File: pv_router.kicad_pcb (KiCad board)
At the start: 4 copper layers, 75 x 69.2 mm, 51 parts, among them IC1 L6981C33DR, IC2 ATM90E26-YU-B, IC3 ESP32-C3-WROOM-02-N4, J1 Barrel_Jack_Switch_Pin3Ring, J2 AudioJack3, J3 AudioJack3, J4 Barrel_Jack_Switch_Pin3Ring, J5 UART, J6 ToSSR, Q1 BSS138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

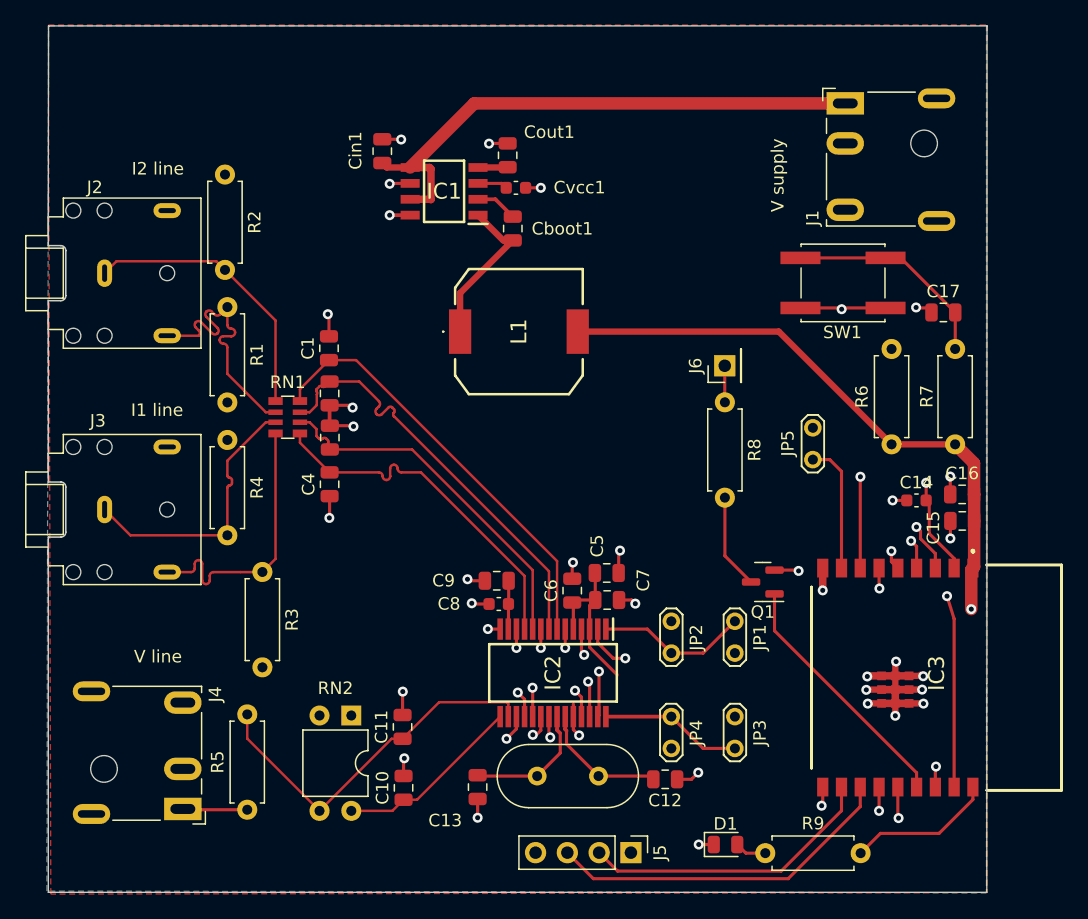
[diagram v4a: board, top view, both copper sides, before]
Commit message: pcb: add GND vias in planes
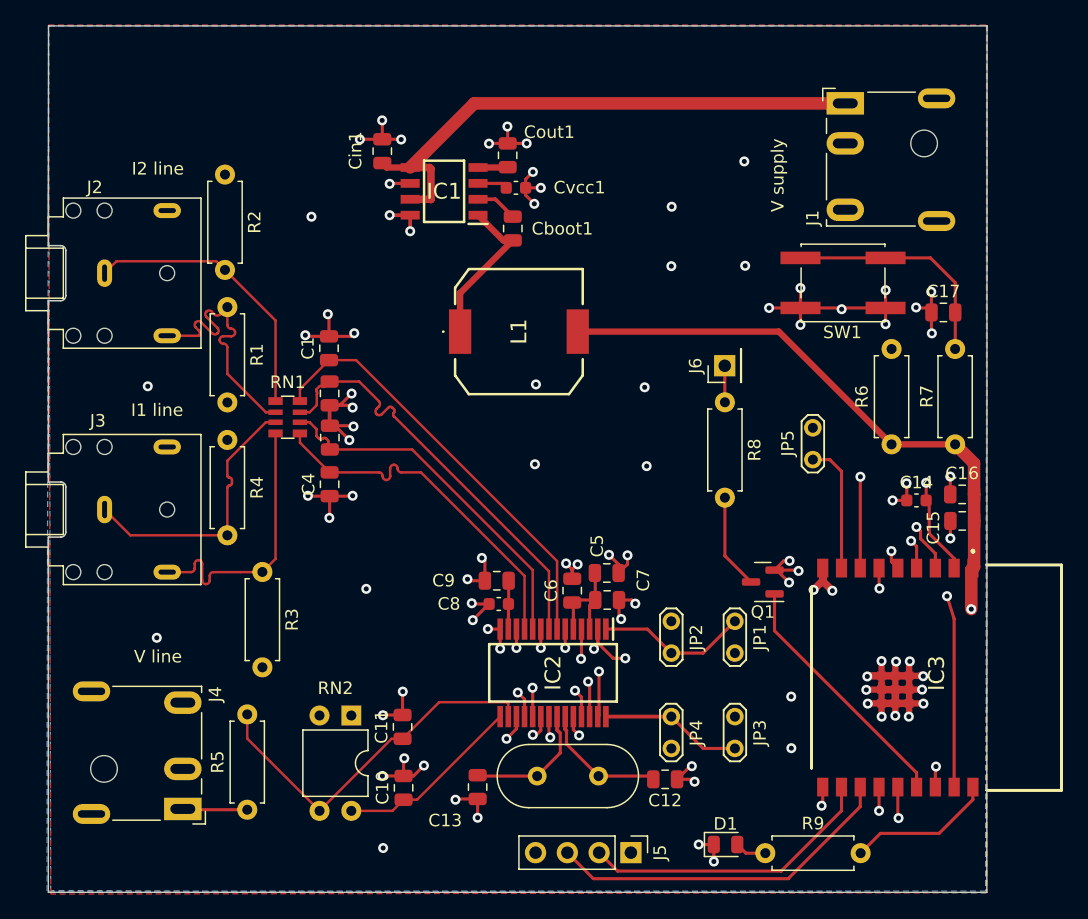
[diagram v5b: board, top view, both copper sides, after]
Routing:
- net GND: track 79.3 -> 150.1 mm, vias 40 -> 96
- net +3V3: track 83.8 -> 79.3 mm
- net /esp32/EN: track 36.5 -> 37.9 mm
- net /adc/RESET: track 53.1 -> 53.8 mm

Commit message: pcb: fix +3.3v plane
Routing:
- net +3V3: track 79.3 -> 8.77 mm, vias 1 -> 0
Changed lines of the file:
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@@
   (arc (start 151.72 116.748959) (mid 151.807868 116.961091) (end 152.02 117.048959) (width 0.2) (layer "F.Cu") (net 5))
   (arc (start 152.62 115.831016) (mid 152.832132 115.918884) (end 152.92 116.131016) (width 0.2) (layer "F.Cu") (net 5))
-  (segment (start 198.76 127.37) (end 198.76 124.22) (width 1) (layer "F.Cu") (net 6))
   (segment (start 168.71 126.64) (end 168.26 127.09) (width 0.25) (layer "F.Cu") (net 6))
   (segment (start 166.96 126.93) (end 166.87 126.84) (width 0.25) (layer "F.Cu") (net 6))
   (segment (start 168.71 124.51) (end 168.68 124.48) (width 0.25) (layer "F.Cu") (net 6))
   (segment (start 167.07 126.64) (end 166.87 126.84) (width 0.25) (layer "F.Cu") (net 6))
-  (segment (start 198.98 115.71) (end 198.98 118.2) (width 1) (layer "F.Cu") (net 6))
-  (segment (start 198.99 120.32) (end 198.99 123.99) (width 1) (layer "F.Cu") (net 6))
-  (segment (start 198.99 118.21) (end 198.98 118.2) (width 1) (layer "F.Cu") (net 6))
-  (segment (start 161.685 92.075) (end 161.71 92.05) (width 0.508) (layer "F.Cu") (net 6))
-  (segment (start 183.38 105.19) (end 192.39 114.2) (width 0.508) (layer "F.Cu") (net 6))
-  (segment (start 197.47 114.2) (end 198.98 115.71) (width 1) (layer "F.Cu") (net 6))
   (segment (start 168.71 126.64) (end 167.07 126.64) (width 0.25) (layer "F.Cu") (net 6))
-  (segment (start 159.342 92.075) (end 161.685 92.075) (width 0.508) (layer "F.Cu") (net 6))
   (segment (start 168.26 127.09) (end 168.26 128.964) (width 0.25) (layer "F.Cu") (net 6))
   (segment (start 166.96 128.964) (end 166.96 126.93) (width 0.25) (layer "F.Cu") (net 6))
-  (segment (start 198.99 123.99) (end 198.89 124.09) (width 1) (layer "F.Cu") (net 6))
   (segment (start 168.71 126.64) (end 168.71 124.51) (width 0.25) (layer "F.Cu") (net 6))
-  (segment (start 198.76 124.22) (end 198.89 124.09) (width 1) (layer "F.Cu") (net 6))
-  (segment (start 198.99 120.32) (end 198.99 118.21) (width 1) (layer "F.Cu") (net 6))
-  (segment (start 192.39 114.2) (end 197.47 114.2) (width 0.508) (layer "F.Cu") (net 6))
-  (segment (start 167.31 105.19) (end 183.38 105.19) (width 0.508) (layer "F.Cu") (net 6))
-  (via (at 198.76 127.37) (size 0.8) (drill 0.4) (layers "F.Cu" "B.Cu") (net 6))
-  (segment (start 187.41 130.88) (end 189.31 128.98) (width 1) (layer "In2.Cu") (net 6))
-  (segment (start 197.15 128.98) (end 198.76 127.37) (width 1) (layer "In2.Cu") (net 6))
-  (segment (start 189.31 128.98) (end 197.15 128.98) (width 1) (layer "In2.Cu") (net 6))
-  (segment (start 179.87 130.88) (end 187.41 130.88) (width 1) (layer "In2.Cu") (net 6))
   (segment (start 161.79 126.945) (end 161.775 126.96) (width 0.25) (layer "F.Cu") (net 7))
   (segment (start 161.775 126.96) (end 161.775 128.949) (width 0.25) (layer "F.Cu") (net 7))

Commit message: pcb: add GND vias to some pads, layer 1
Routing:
- net GND: track 150.1 -> 153.8 mm, vias 96 -> 98
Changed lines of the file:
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@@
     (effects (font (size 1 1) (thickness 0.15)) (justify left bottom))
   )
+  (segment (start 165.66 123.53) (end 165.66 128.964) (width 0.2) (layer "F.Cu") (net 1))
   (segment (start 145.11 109.79) (end 147.43 107.47) (width 0.2) (layer "F.Cu") (net 1))
   (segment (start 145.11 110.74) (end 145.11 109.79) (width 0.2) (layer "F.Cu") (net 1))
-  (segment (start 165.66 123.53) (end 149.6 107.47) (width 0.2) (layer "F.Cu") (net 1))
-  (segment (start 165.66 128.964) (end 165.66 123.53) (width 0.2) (layer "F.Cu") (net 1))
-  (segment (start 149.6 107.47) (end 147.43 107.47) (width 0.2) (layer "F.Cu") (net 1))
+  (segment (start 147.43 107.47) (end 149.6 107.47) (width 0.2) (layer "F.Cu") (net 1))
+  (segment (start 149.6 107.47) (end 165.66 123.53) (width 0.2) (layer "F.Cu") (net 1))
   (segment (start 192.69 134.9) (end 193.1131 134.9) (width 0.25) (layer "F.Cu") (net 2))
   (segment (start 175.25 140.97) (end 176.46 140.97) (width 0.25) (layer "F.Cu") (net 2))
@@
   (segment (start 163.99 93.7) (end 164.359998 93.7) (width 0.25) (layer "F.Cu") (net 2))
   (segment (start 193.79 135.94) (end 193.77 135.96) (width 0.508) (layer "F.Cu") (net 2))
+  (segment (start 175.25 140.97) (end 175.25 142.82) (width 0.25) (layer "F.Cu") (net 2))
   (segment (start 171.29 123.77) (end 171.29 123.07) (width 0.25) (layer "F.Cu") (net 2))
   (segment (start 147.48 120.06) (end 147.46 120.08) (width 0.25) (layer "F.Cu") (net 2))
@@
   (segment (start 194.83 133.8) (end 194.830012 133.800012) (width 0.25) (layer "F.Cu") (net 2))
   (segment (start 178.1825 146.18) (end 176.98 146.18) (width 0.25) (layer "F.Cu") (net 2))
+  (segment (start 175.25 142.82) (end 175.22 142.85) (width 0.25) (layer "F.Cu") (net 2))
   (segment (start 184.895 124.25) (end 184.96 124.315) (width 0.25) (layer "F.Cu") (net 2))
   (segment (start 193.79 134.9) (end 193.79 135.94) (width 0.508) (layer "F.Cu") (net 2))
@@
   (segment (start 161.71 90.15) (end 160.24 90.15) (width 0.25) (layer "F.Cu") (net 2))
   (segment (start 148.3 111.08) (end 149.24 110.14) (width 0.25) (layer "F.Cu") (net 2))
+  (segment (start 159.31 142.54) (end 161.15 142.54) (width 0.25) (layer "F.Cu") (net 2))
   (segment (start 168.91 130.25) (end 168.91 128.964) (width 0.25) (layer "F.Cu") (net 2))
   (segment (start 149.2 105.57) (end 149.45 105.32) (width 0.25) (layer "F.Cu") (net 2))
@@
   (via (at 163.73 92.43) (size 0.8) (drill 0.4) (layers "F.Cu" "B.Cu") (net 2))
   (via (at 149.45 105.32) (size 0.8) (drill 0.4) (layers "F.Cu" "B.Cu") (free) (net 2))
+  (via (at 175.22 142.85) (size 0.8) (drill 0.4) (layers "F.Cu" "B.Cu") (net 2))
   (via (at 149.39 112.77) (size 0.8) (drill 0.4) (layers "F.Cu" "B.Cu") (free) (net 2))
   (via (at 184.2 125.24) (size 0.8) (drill 0.4) (layers "F.Cu" "B.Cu") (net 2))
@@
   (via (at 170.78 128.16) (size 0.8) (drill 0.4) (layers "F.Cu" "B.Cu") (net 2))
   (via (at 163.97 109.41) (size 0.8) (drill 0.4) (layers "F.Cu" "B.Cu") (free) (net 2))
+  (via (at 161.15 142.54) (size 0.8) (drill 0.4) (layers "F.Cu" "B.Cu") (net 2))
   (via (at 158.5 124.98) (size 0.8) (drill 0.4) (layers "F.Cu" "B.Cu") (free) (net 2))
   (via (at 167.42 137.46) (size 0.8) (drill 0.4) (layers "F.Cu" "B.Cu") (net 2))
   (via (at 167.299552 123.793071) (size 0.8) (drill 0.4) (layers "F.Cu" "B.Cu") (net 2))
-  (segment (start 151.419999 111.174265) (end 151.42 111.174264) (width 0.2) (layer "F.Cu") (net 3))
-  (segment (start 152.621794 111.951795) (end 165.01 124.34) (width 0.2) (layer "F.Cu") (net 3))
   (segment (start 145.11 111.635) (end 145.37 111.635) (width 0.2) (layer "F.Cu") (net 3))
   (segment (start 147.090033 109.569969) (end 147.48 109.18) (width 0.2) (layer "F.Cu") (net 3))
-  (segment (start 151.233449 111.78508) (end 151.233448 111.785079) (width 0.2) (layer "F.Cu") (net 3))
+  (segment (start 151.42 111.174264) (end 151.233448 111.360815) (width 0.2) (layer "F.Cu") (net 3))
   (segment (start 152.621793 111.951794) (end 152.621794 111.951795) (width 0.2) (layer "F.Cu") (net 3))
-  (segment (start 152.479802 111.245258) (end 152.621794 111.38725) (width 0.2) (layer "F.Cu") (net 3))
   (segment (start 146.455 111.065) (end 146.455 110.205) (width 0.2) (layer "F.Cu") (net 3))
-  (segment (start 151.657713 111.785078) (end 151.657712 111.785079) (width 0.2) (layer "F.Cu") (net 3))
   (segment (start 146.455002 109.783465) (end 146.455 109.783466) (width 0.2) (layer "F.Cu") (net 3))
-  (segment (start 152.621795 111.669521) (end 152.621794 111.669522) (width 0.2) (layer "F.Cu") (net 3))
+  (segment (start 149.85 109.18) (end 151.42 110.75) (width 0.2) (layer "F.Cu") (net 3))
+  (segment (start 152.621794 111.951795) (end 165.01 124.34) (width 0.2) (layer "F.Cu") (net 3))
   (segment (start 152.621794 111.669522) (end 152.621794 111.669523) (width 0.2) (layer "F.Cu") (net 3))
   (segment (start 147.48 109.18) (end 149.85 109.18) (width 0.2) (layer "F.Cu") (net 3))
+  (segment (start 151.657713 111.785078) (end 151.657712 111.785079) (width 0.2) (layer "F.Cu") (net 3))
+  (segment (start 146.455 109.783466) (end 146.668499 109.569968) (width 0.2) (layer "F.Cu") (net 3))
+  (segment (start 151.233449 111.78508) (end 151.233448 111.785079) (width 0.2) (layer "F.Cu") (net 3))
+  (segment (start 151.419999 111.174265) (end 151.42 111.174264) (width 0.2) (layer "F.Cu") (net 3))
+  (segment (start 146.455 109.994234) (end 146.455001 109.994232) (width 0.2) (layer "F.Cu") (net 3))
+  (segment (start 147.090032 109.56997) (end 147.090033 109.569969) (width 0.2) (layer "F.Cu") (net 3))
+  (segment (start 152.479802 111.245258) (end 152.621794 111.38725) (width 0.2) (layer "F.Cu") (net 3))
+  (segment (start 145.885 111.635) (end 146.455 111.065) (width 0.2) (layer "F.Cu") (net 3))
+  (segment (start 145.11 111.635) (end 145.885 111.635) (width 0.2) (layer "F.Cu") (net 3))
+  (segment (start 146.879267 109.569968) (end 146.879265 109.569969) (width 0.2) (layer "F.Cu") (net 3))
+  (segment (start 151.657712 111.785079) (end 152.19753 111.245257) (width 0.2) (layer "F.Cu") (net 3))
   (segment (start 152.479804 111.245259) (end 152.479802 111.245258) (width 0.2) (layer "F.Cu") (net 3))
-  (segment (start 146.455 109.783466) (end 146.668499 109.569968) (width 0.2) (layer "F.Cu") (net 3))
-  (segment (start 151.42 111.174264) (end 151.233448 111.360815) (width 0.2) (layer "F.Cu") (net 3))
-  (segment (start 146.455 109.994234) (end 146.455001 109.994232) (width 0.2) (layer "F.Cu") (net 3))
   (segment (start 165.01 124.34) (end 165.01 128.964) (width 0.2) (layer "F.Cu") (net 3))
-  (segment (start 147.090032 109.56997) (end 147.090033 109.569969) (width 0.2) (layer "F.Cu") (net 3))
-  (segment (start 145.885 111.635) (end 146.455 111.065) (width 0.2) (layer "F.Cu") (net 3))
-  (segment (start 149.85 109.18) (end 151.42 110.75) (width 0.2) (layer "F.Cu") (net 3))
-  (segment (start 145.11 111.635) (end 145.885 111.635) (width 0.2) (layer "F.Cu") (net 3))
-  (segment (start 151.657712 111.785079) (end 152.19753 111.245257) (width 0.2) (layer "F.Cu") (net 3))
-  (segment (start 146.879267 109.569968) (end 146.879265 109.569969) (width 0.2) (layer "F.Cu") (net 3))
+  (segment (start 152.621795 111.669521) (end 152.621794 111.669522) (width 0.2) (layer "F.Cu") (net 3))
   (arc (start 146.455 110.205) (mid 146.498651 110.099617) (end 146.455 109.994234) (width 0.2) (layer "F.Cu") (net 3))
-  (arc (start 152.19753 111.245257) (mid 152.338668 111.186799) (end 152.479804 111.245259) (width 0.2) (layer "F.Cu") (net 3))
   (arc (start 146.668499 109.569968) (mid 146.773882 109.526318) (end 146.879267 109.569968) (width 0.2) (layer "F.Cu") (net 3))
   (arc (start 146.879265 109.569969) (mid 146.984649 109.61362) (end 147.090032 109.56997) (width 0.2) (layer "F.Cu") (net 3))
+  (arc (start 151.42 110.75) (mid 151.507868 110.962133) (end 151.419999 111.174265) (width 0.2) (layer "F.Cu") (net 3))
+  (arc (start 151.233448 111.360815) (mid 151.14558 111.572948) (end 151.233449 111.78508) (width 0.2) (layer "F.Cu") (net 3))
   (arc (start 146.455001 109.994232) (mid 146.411349 109.888849) (end 146.455002 109.783465) (width 0.2) (layer "F.Cu") (net 3))
   (arc (start 152.621794 111.669523) (mid 152.563333 111.810658) (end 152.621793 111.951794) (width 0.2) (layer "F.Cu") (net 3))
-  (arc (start 151.42 110.75) (mid 151.507868 110.962133) (end 151.419999 111.174265) (width 0.2) (layer "F.Cu") (net 3))
-  (arc (start 151.233448 111.360815) (mid 151.14558 111.572948) (end 151.233449 111.78508) (width 0.2) (layer "F.Cu") (net 3))
   (arc (start 152.621794 111.38725) (mid 152.680255 111.528385) (end 152.621795 111.669521) (width 0.2) (layer "F.Cu") (net 3))
   (arc (start 151.233448 111.785079) (mid 151.445581 111.872947) (end 151.657713 111.785078) (width 0.2) (layer "F.Cu") (net 3))
+  (arc (start 152.19753 111.245257) (mid 152.338668 111.186799) (end 152.479804 111.245259) (width 0.2) (layer "F.Cu") (net 3))
   (segment (start 147.347033 114.164263) (end 147.347034 114.164265) (width 0.2) (layer "F.Cu") (net 4))
   (segment (start 147.347034 114.457035) (end 147.478528 114.588528) (width 0.2) (layer "F.Cu") (net 4))

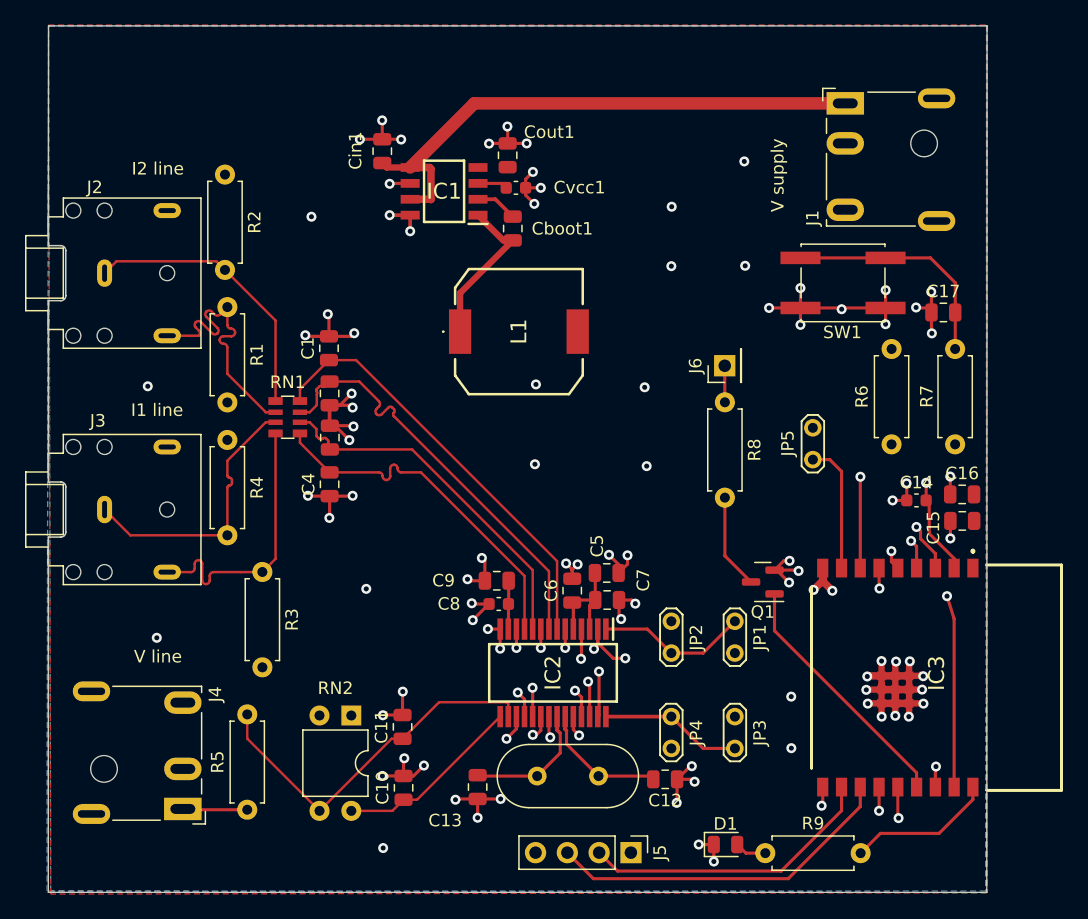
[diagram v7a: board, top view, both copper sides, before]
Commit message: fix: barrel jack FP on PCB
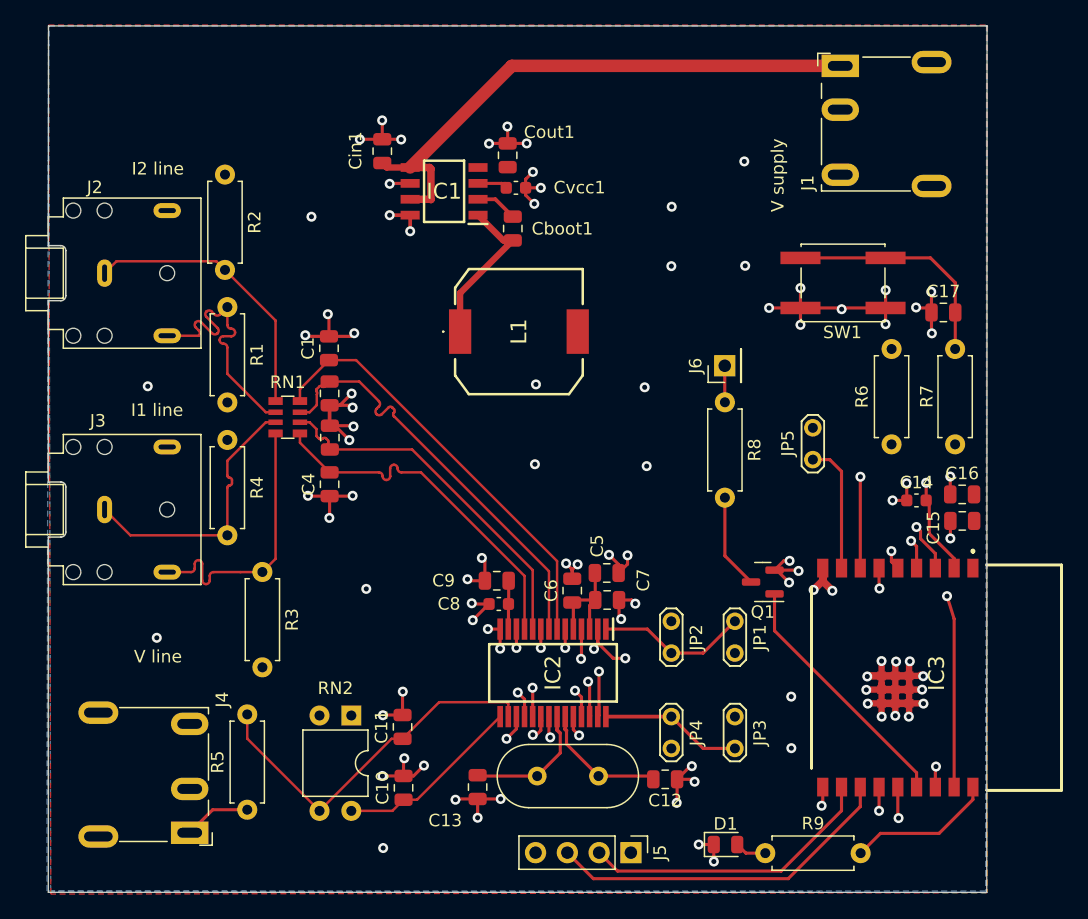
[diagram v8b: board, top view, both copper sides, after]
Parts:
- J1, J4: footprint Connector_BarrelJack:BarrelJack_CUI_PJ-079BH_Horizontal -> BarrelJack:BarrelJack_CUI_PJ-051A_Horizontal
- moved J4 5.94 mm to (130.0, 141.8)
- moved J1 5.91 mm to (194.6, 87.4)
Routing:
- net Net-(IC1-EN/CLKIN): track 45.1 -> 45.9 mm
